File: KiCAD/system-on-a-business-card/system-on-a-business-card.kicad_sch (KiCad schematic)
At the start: 15 parts, among them J1 USB_C_Receptacle, J3 Conn_01x04_Socket, SW1 SW_Push, U1 USBLC6-2SC6

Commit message: #10: separated reset and display reset signals, added pull-up to display reset
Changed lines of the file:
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@@
   (junction (at 250.19 127) (diameter 0) (color 0 0 0 0)
-  )
-  (junction (at 115.57 50.8) (diameter 0) (color 0 0 0 0)
   )
   (no_connect (at 66.04 157.48))
@@
     (stroke (width 0) (type default))
   )
-  (wire (pts (xy 111.76 50.8) (xy 115.57 50.8))
-    (stroke (width 0) (type default))
-  )
   (wire (pts (xy 195.58 71.12) (xy 199.39 71.12))
     (stroke (width 0) (type default))
@@
     (stroke (width 0) (type default))
   )
-  (global_label "RESET" (shape output) (at 111.76 50.8 180) (fields_autoplaced)
-    (effects (font (size 1.27 1.27)) (justify right))
-    (property "Intersheetrefs" "${INTERSHEET_REFS}" (at 103.0297 50.8 0)
-      (effects (font (size 1.27 1.27)) (justify right) hide)
-    )
-  )
   (global_label "UART_RXD" (shape input) (at 195.58 66.04 180) (fields_autoplaced)

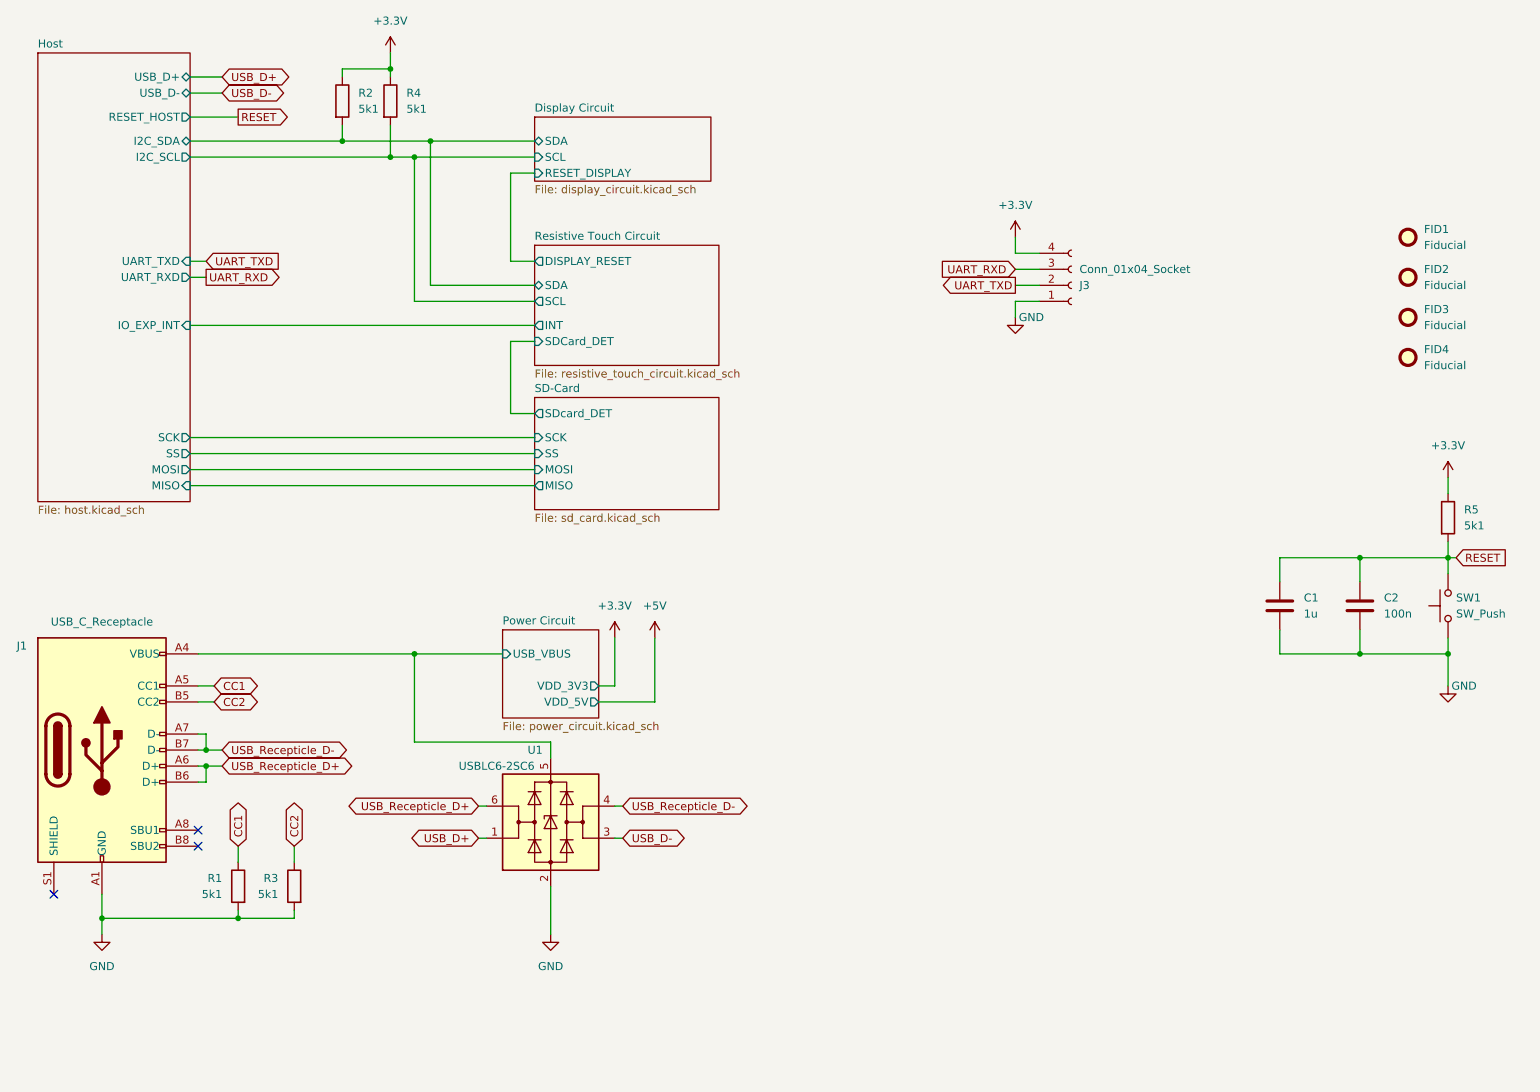
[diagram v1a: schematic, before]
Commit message: #10: created version with DAC, Op Amp and speaker
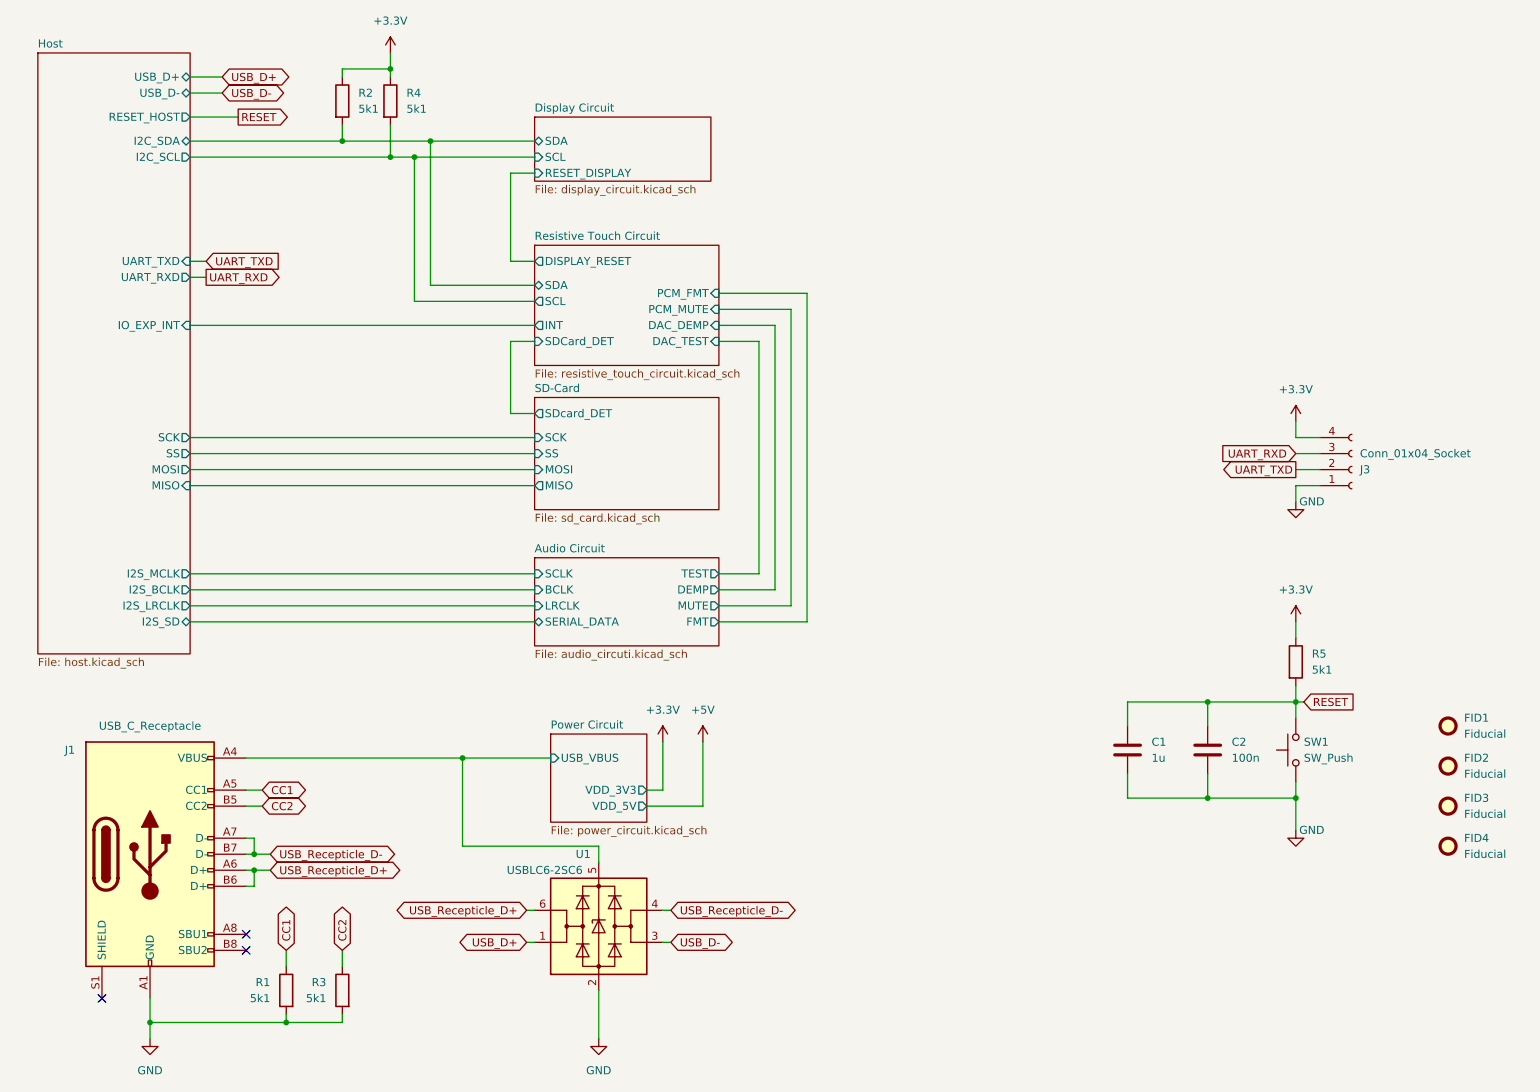
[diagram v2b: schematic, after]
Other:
- added sheet Audio Circuit (audio_circuti.kicad_sch)
- sheet Host ports: added I2S_BCLK, I2S_LRCLK, I2S_MCLK, I2S_SD; removed none
- sheet Resistive Touch Circuit ports: added DAC_DEMP, DAC_TEST, PCM_FMT, PCM_MUTE; removed none
- moved on the sheet: C1, C2, FID1, FID2, FID3, FID4, J1, J3, R1, R3, R5, SW1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
